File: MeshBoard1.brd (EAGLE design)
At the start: 54.7 x 18.6 mm, 6 parts

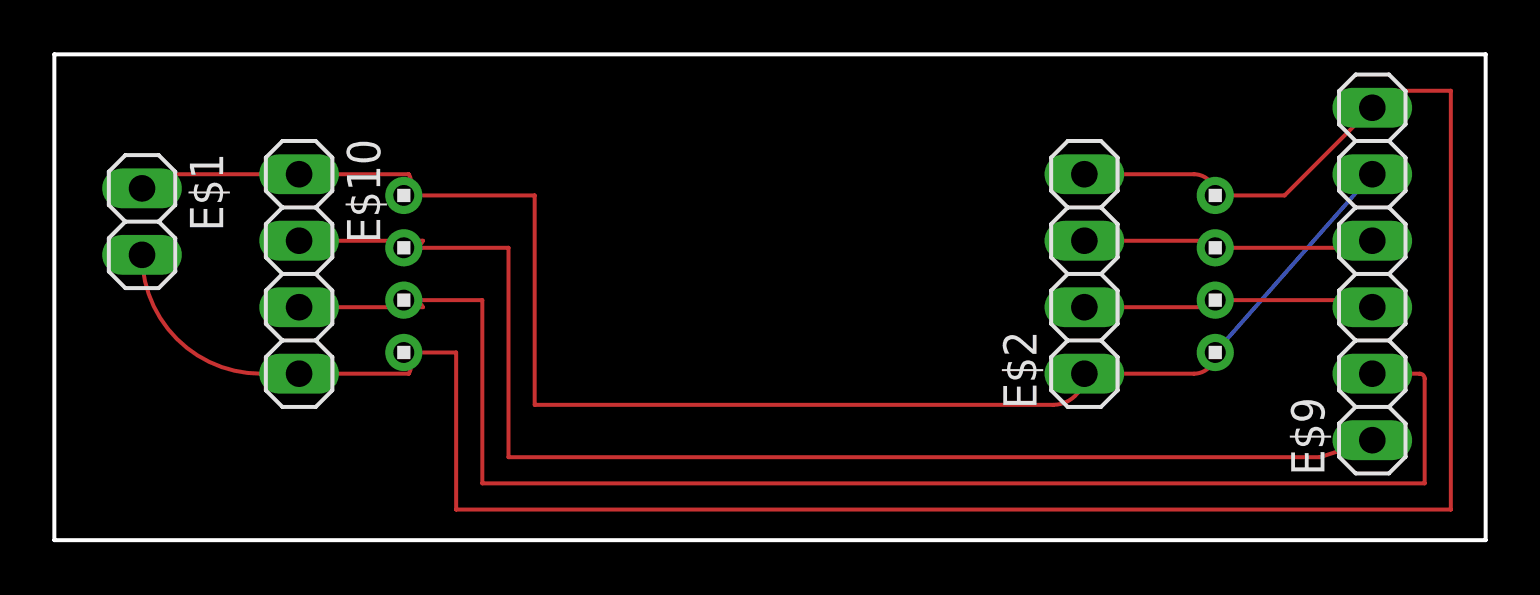
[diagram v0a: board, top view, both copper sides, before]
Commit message: Better description of channels/freq
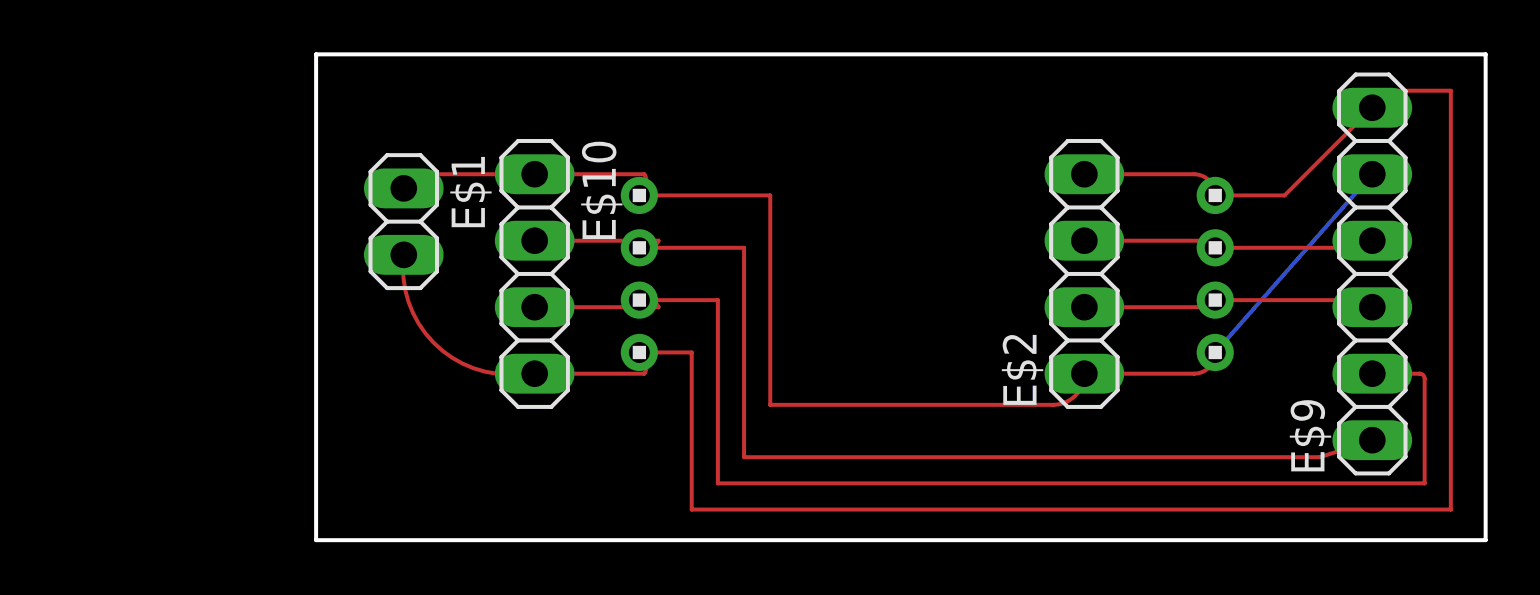
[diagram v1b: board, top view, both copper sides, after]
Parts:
- moved E$1 10.0 mm to (10.0, 62.0)
- moved E$10 9.00 mm to (15.0, 60.0)
- moved E$3 9.00 mm to (19.0, 60.0)
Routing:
- net S$2: track 60.2 -> 50.2 mm
- net S$1: track 90.9 -> 81.2 mm
- net S$6: track 57.6 -> 48.6 mm
- net S$5: track 50.6 -> 41.6 mm
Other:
- board size 54.7 x 18.6 mm -> 44.7 x 18.6 mm
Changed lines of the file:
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@@
 <board>
 <plain>
-<wire x1="-3.35" y1="68.39" x2="51.33" y2="68.39" width="0.1524" layer="20"/>
+<wire x1="6.65" y1="68.39" x2="51.33" y2="68.39" width="0.1524" layer="20"/>
 <wire x1="51.33" y1="68.39" x2="51.33" y2="49.83" width="0.1524" layer="20"/>
-<wire x1="51.33" y1="49.83" x2="-3.35" y2="49.83" width="0.1524" layer="20"/>
-<wire x1="-3.35" y1="49.83" x2="-3.35" y2="68.39" width="0.1524" layer="20"/>
+<wire x1="51.33" y1="49.83" x2="6.65" y2="49.83" width="0.1524" layer="20"/>
+<wire x1="6.65" y1="49.83" x2="6.65" y2="68.39" width="0.1524" layer="20"/>
 </plain>
 <attributes>
@@
 <elements>
 <element name="E$9" library="pinhead" library_urn="urn:adsk.eagle:library:325" package="1X06" package3d_urn="urn:adsk.eagle:package:22472/2" value="" x="47" y="60" rot="R90"/>
-<element name="E$10" library="pinhead" library_urn="urn:adsk.eagle:library:325" package="1X04" package3d_urn="urn:adsk.eagle:package:22407/2" value="" x="6" y="60" rot="R270"/>
-<element name="E$1" library="pinhead" library_urn="urn:adsk.eagle:library:325" package="1X02" package3d_urn="urn:adsk.eagle:package:22435/2" value="" x="0" y="62" rot="R270"/>
+<element name="E$10" library="pinhead" library_urn="urn:adsk.eagle:library:325" package="1X04" package3d_urn="urn:adsk.eagle:package:22407/2" value="" x="15" y="60" rot="R270"/>
+<element name="E$1" library="pinhead" library_urn="urn:adsk.eagle:library:325" package="1X02" package3d_urn="urn:adsk.eagle:package:22435/2" value="" x="10" y="62" rot="R270"/>
 <element name="E$2" library="pinhead" library_urn="urn:adsk.eagle:library:325" package="1X04" package3d_urn="urn:adsk.eagle:package:22407/2" value="" x="36" y="60" rot="R90"/>
-<element name="E$3" library="headers(2mm)" package="1X4" value="" x="10" y="60" rot="R270"/>
+<element name="E$3" library="headers(2mm)" package="1X4" value="" x="19" y="60" rot="R270"/>
 <element name="E$4" library="headers(2mm)" package="1X4" value="" x="41" y="60" rot="R270"/>
 </elements>
@@
 <contactref element="E$3" pad="4"/>
 <contactref element="E$4" pad="1"/>
-<wire x1="0" y1="60.73" x2="4.54" y2="56.19" width="0.1524" layer="1" curve="90"/>
-<wire x1="4.54" y1="56.19" x2="6" y2="56.19" width="0.1524" layer="1"/>
-<wire x1="6" y1="56.19" x2="10.19" y2="56.19" width="0.1524" layer="1"/>
-<wire x1="10.19" y1="56.19" x2="10" y2="57" width="0.1524" layer="1" curve="90"/>
+<wire x1="10" y1="60.73" x2="13.54" y2="56.19" width="0.1524" layer="1" curve="90"/>
+<wire x1="13.54" y1="56.19" x2="15" y2="56.19" width="0.1524" layer="1"/>
+<wire x1="15" y1="56.19" x2="19.19" y2="56.19" width="0.1524" layer="1"/>
+<wire x1="19.19" y1="56.19" x2="19" y2="57" width="0.1524" layer="1" curve="90"/>
 <wire x1="36" y1="63.81" x2="40.19" y2="63.81" width="0.1524" layer="1"/>
 <wire x1="40.19" y1="63.81" x2="41" y2="63" width="0.1524" layer="1" curve="-90"/>
 <wire x1="41" y1="63" x2="43.65" y2="63" width="0.1524" layer="1"/>
 <wire x1="43.65" y1="63" x2="47" y2="66.35" width="0.1524" layer="1"/>
-<wire x1="10" y1="57" x2="12" y2="57" width="0.1524" layer="1"/>
-<wire x1="12" y1="57" x2="12" y2="51" width="0.1524" layer="1"/>
-<wire x1="12" y1="51" x2="50" y2="51" width="0.1524" layer="1"/>
+<wire x1="19" y1="57" x2="21" y2="57" width="0.1524" layer="1"/>
+<wire x1="21" y1="57" x2="21" y2="51" width="0.1524" layer="1"/>
+<wire x1="21" y1="51" x2="50" y2="51" width="0.1524" layer="1"/>
 <wire x1="50" y1="51" x2="50" y2="67" width="0.1524" layer="1"/>
 <wire x1="50" y1="67" x2="47.65" y2="67" width="0.1524" layer="1"/>
@@
 <contactref element="E$3" pad="1"/>
 <contactref element="E$4" pad="4"/>
-<wire x1="0" y1="63.27" x2="0.54" y2="63.81" width="0.1524" layer="1" curve="-90"/>
-<wire x1="0.54" y1="63.81" x2="6" y2="63.81" width="0.1524" layer="1"/>
-<wire x1="6" y1="63.81" x2="10.19" y2="63.81" width="0.1524" layer="1"/>
-<wire x1="10.19" y1="63.81" x2="10" y2="63" width="0.1524" layer="1" curve="-90"/>
+<wire x1="10" y1="63.27" x2="10.54" y2="63.81" width="0.1524" layer="1" curve="-90"/>
+<wire x1="10.54" y1="63.81" x2="15" y2="63.81" width="0.1524" layer="1"/>
+<wire x1="15" y1="63.81" x2="19.19" y2="63.81" width="0.1524" layer="1"/>
+<wire x1="19.19" y1="63.81" x2="19" y2="63" width="0.1524" layer="1" curve="-90"/>
 <wire x1="36" y1="56.19" x2="40.19" y2="56.19" width="0.1524" layer="1"/>
 <wire x1="40.19" y1="56.19" x2="41" y2="57" width="0.1524" layer="1" curve="90"/>
 <wire x1="41" y1="57" x2="47" y2="63.81" width="0.1524" layer="16"/>
-<wire x1="10" y1="63" x2="15" y2="63" width="0.1524" layer="1"/>
-<wire x1="15" y1="63" x2="15" y2="55" width="0.1524" layer="1"/>
+<wire x1="19" y1="63" x2="24" y2="63" width="0.1524" layer="1"/>
+<wire x1="24" y1="63" x2="24" y2="55" width="0.1524" layer="1"/>
 <wire x1="34.81" y1="55" x2="36" y2="56.19" width="0.1524" layer="1" curve="90"/>
-<wire x1="15" y1="55" x2="34.81" y2="55" width="0.1524" layer="1"/>
+<wire x1="24" y1="55" x2="34.81" y2="55" width="0.1524" layer="1"/>
 </signal>
 <signal name="S$3">
@@
 <contactref element="E$10" pad="2"/>
 <contactref element="E$3" pad="2"/>
-<wire x1="6" y1="61.27" x2="10.73" y2="61.27" width="0.1524" layer="1"/>
-<wire x1="10.73" y1="61.27" x2="10" y2="61" width="0.1524" layer="1" curve="-90"/>
-<wire x1="10" y1="61" x2="14" y2="61" width="0.1524" layer="1"/>
-<wire x1="14" y1="61" x2="14" y2="53" width="0.1524" layer="1"/>
-<wire x1="14" y1="53" x2="45" y2="53" width="0.1524" layer="1"/>
+<wire x1="15" y1="61.27" x2="19.73" y2="61.27" width="0.1524" layer="1"/>
+<wire x1="19.73" y1="61.27" x2="19" y2="61" width="0.1524" layer="1" curve="-90"/>
+<wire x1="19" y1="61" x2="23" y2="61" width="0.1524" layer="1"/>
+<wire x1="23" y1="61" x2="23" y2="53" width="0.1524" layer="1"/>
+<wire x1="23" y1="53" x2="45" y2="53" width="0.1524" layer="1"/>
 <wire x1="45" y1="53" x2="47" y2="53.65" width="0.1524" layer="1"/>
 </signal>
@@
 <contactref element="E$10" pad="3"/>
 <contactref element="E$3" pad="3"/>
-<wire x1="6" y1="58.73" x2="10.73" y2="58.73" width="0.1524" layer="1"/>
-<wire x1="10.73" y1="58.73" x2="10" y2="59" width="0.1524" layer="1" curve="90"/>
-<wire x1="10" y1="59" x2="13" y2="59" width="0.1524" layer="1"/>
-<wire x1="13" y1="59" x2="13" y2="52" width="0.1524" layer="1"/>
-<wire x1="13" y1="52" x2="49" y2="52" width="0.1524" layer="1"/>
+<wire x1="15" y1="58.73" x2="19.73" y2="58.73" width="0.1524" layer="1"/>
+<wire x1="19.73" y1="58.73" x2="19" y2="59" width="0.1524" layer="1" curve="90"/>
+<wire x1="19" y1="59" x2="22" y2="59" width="0.1524" layer="1"/>
+<wire x1="22" y1="59" x2="22" y2="52" width="0.1524" layer="1"/>
+<wire x1="22" y1="52" x2="49" y2="52" width="0.1524" layer="1"/>
 <wire x1="49" y1="52" x2="49" y2="56" width="0.1524" layer="1"/>
 <wire x1="49" y1="56" x2="48.81" y2="56.19" width="0.1524" layer="1" curve="90"/>
